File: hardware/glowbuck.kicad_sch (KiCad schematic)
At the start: 51 parts, among them J1 Conn_01x04_Socket, J101 Conn_01x01_Pin, J102 Conn_01x01_Pin, J105 Conn_01x01_Pin, J106 Conn_01x01_Pin, J107 Conn_01x01_Pin, J3 Conn_02x08_Counter_Clockwise, SW101 SW_Push, SW102 SW_Push, U101 ESP32-S3-WROOM-1

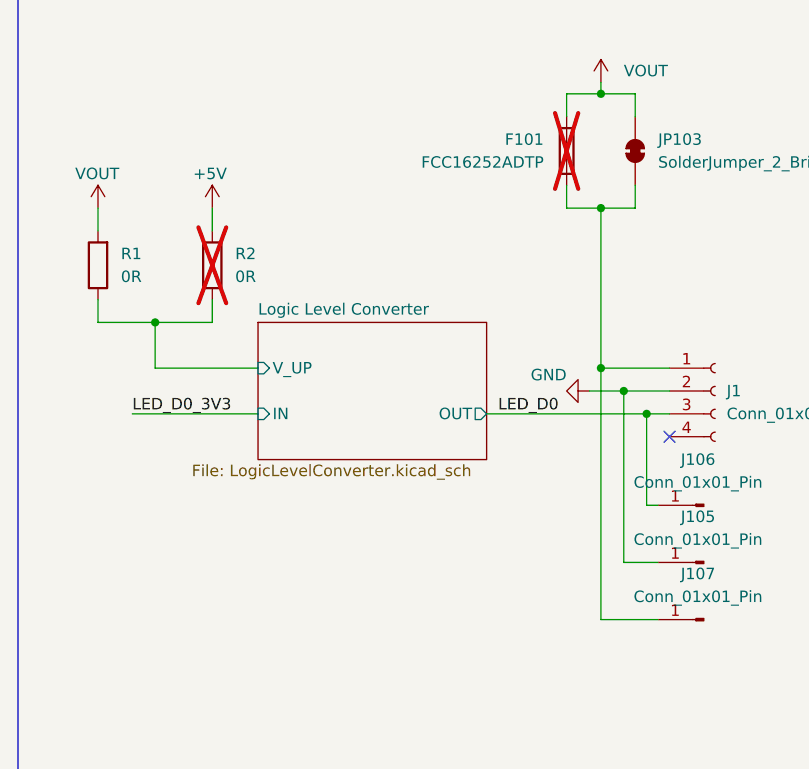
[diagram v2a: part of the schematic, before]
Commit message: Changed footprints to non hand solder option
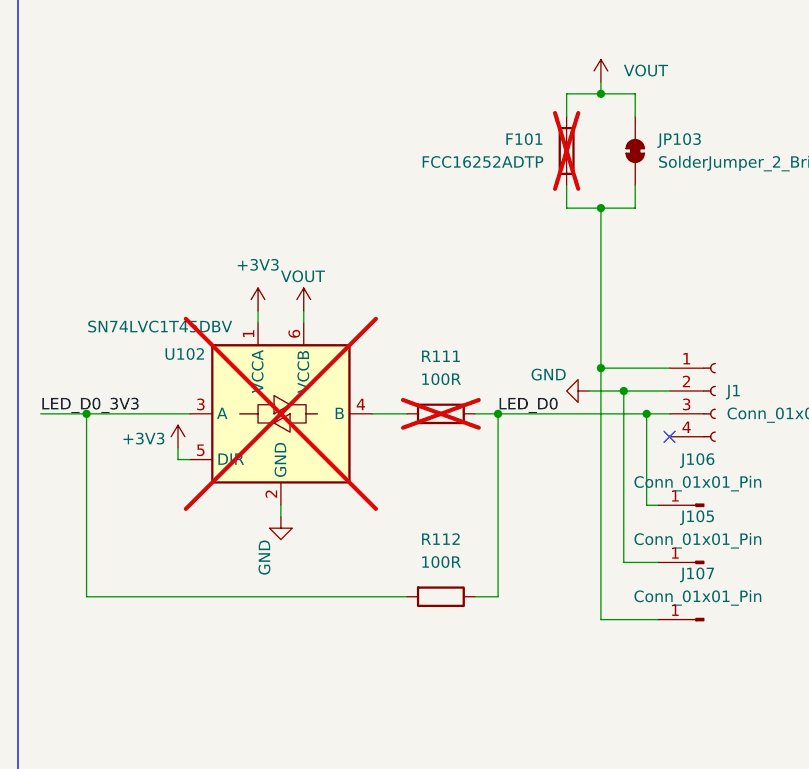
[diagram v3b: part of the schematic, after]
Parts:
- removed R1, R2: 0R, Resistor_SMD:R_0603_1608Metric_Pad0.98x0.95mm_HandSolder, symbol Device:R
- added R111, R112: 100R, Resistor_SMD:R_0603_1608Metric, symbol Device:R
- added U102: SN74LVC1T45DBV, Package_TO_SOT_SMD:SOT-23-6, symbol Logic_LevelTranslator:SN74LVC1T45DBV
- C101, C102, C103, C104, C105: footprint Capacitor_SMD:C_0603_1608Metric_Pad1.08x0.95mm_HandSolder -> Capacitor_SMD:C_0603_1608Metric
- D103: footprint LED_SMD:LED_0603_1608Metric_Pad1.05x0.95mm_HandSolder -> LED_SMD:LED_0603_1608Metric
- D104: footprint Diode_SMD:D_1206_3216Metric_Pad1.42x1.75mm_HandSolder -> Diode_SMD:D_1206_3216Metric
- R101, R102, R103, R104, R105, R106, R107, R108, R109, R110: footprint Resistor_SMD:R_0603_1608Metric_Pad0.98x0.95mm_HandSolder -> Resistor_SMD:R_0603_1608Metric
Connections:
- net +3V3: now also U102.1 (VCCA), U102.5 (DIR)
- net GND: now also U102.2 (GND)
- net LED_D0: now also R111.1, R112.1
- net LED_D0_3V3: now also R112.2, U102.3 (A)
- net VOUT: now also U102.6 (VCCB)
- new net: R111.2, U102.4 (B)
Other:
- removed sheet Logic Level Converter

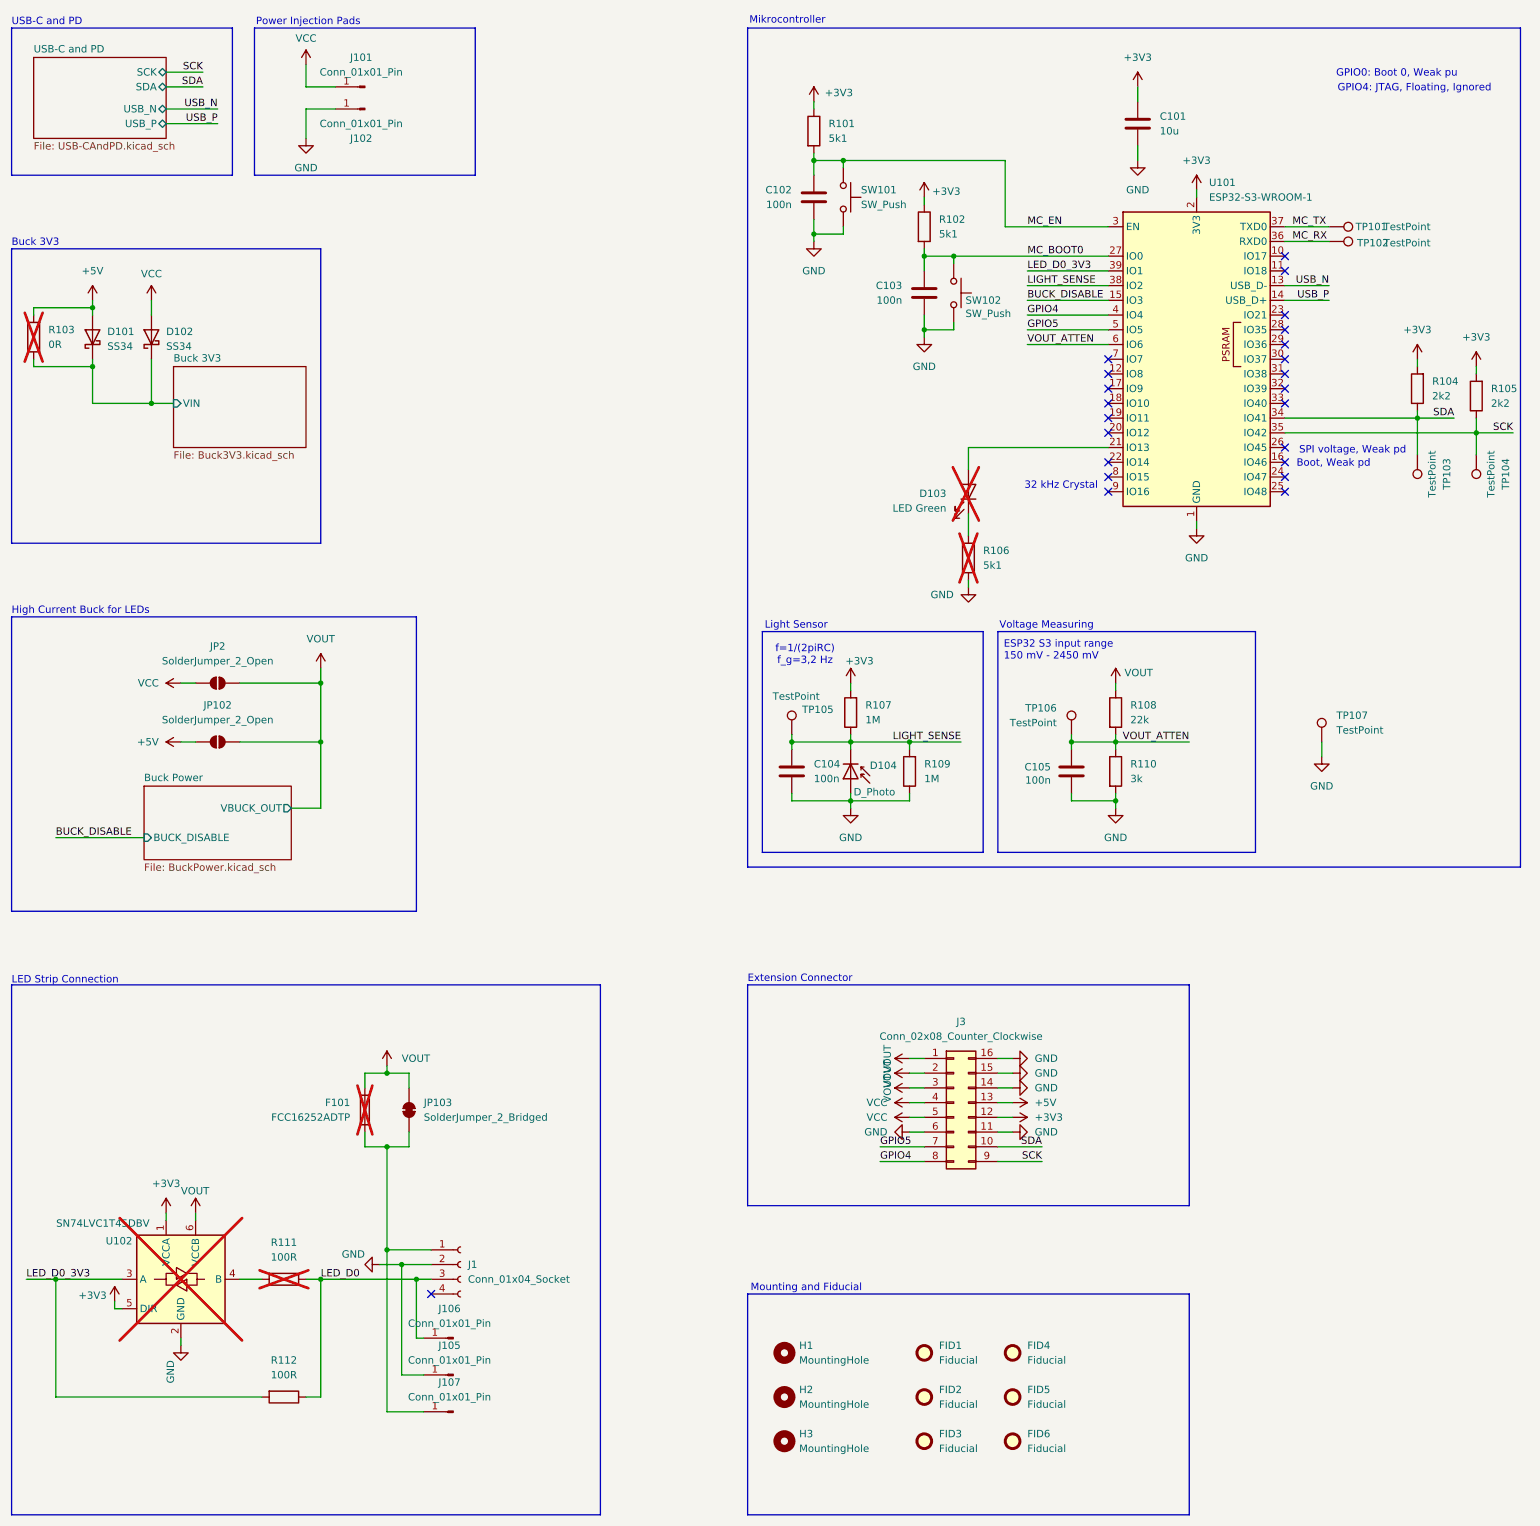
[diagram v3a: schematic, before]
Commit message: Colored nets and added optional current measurement
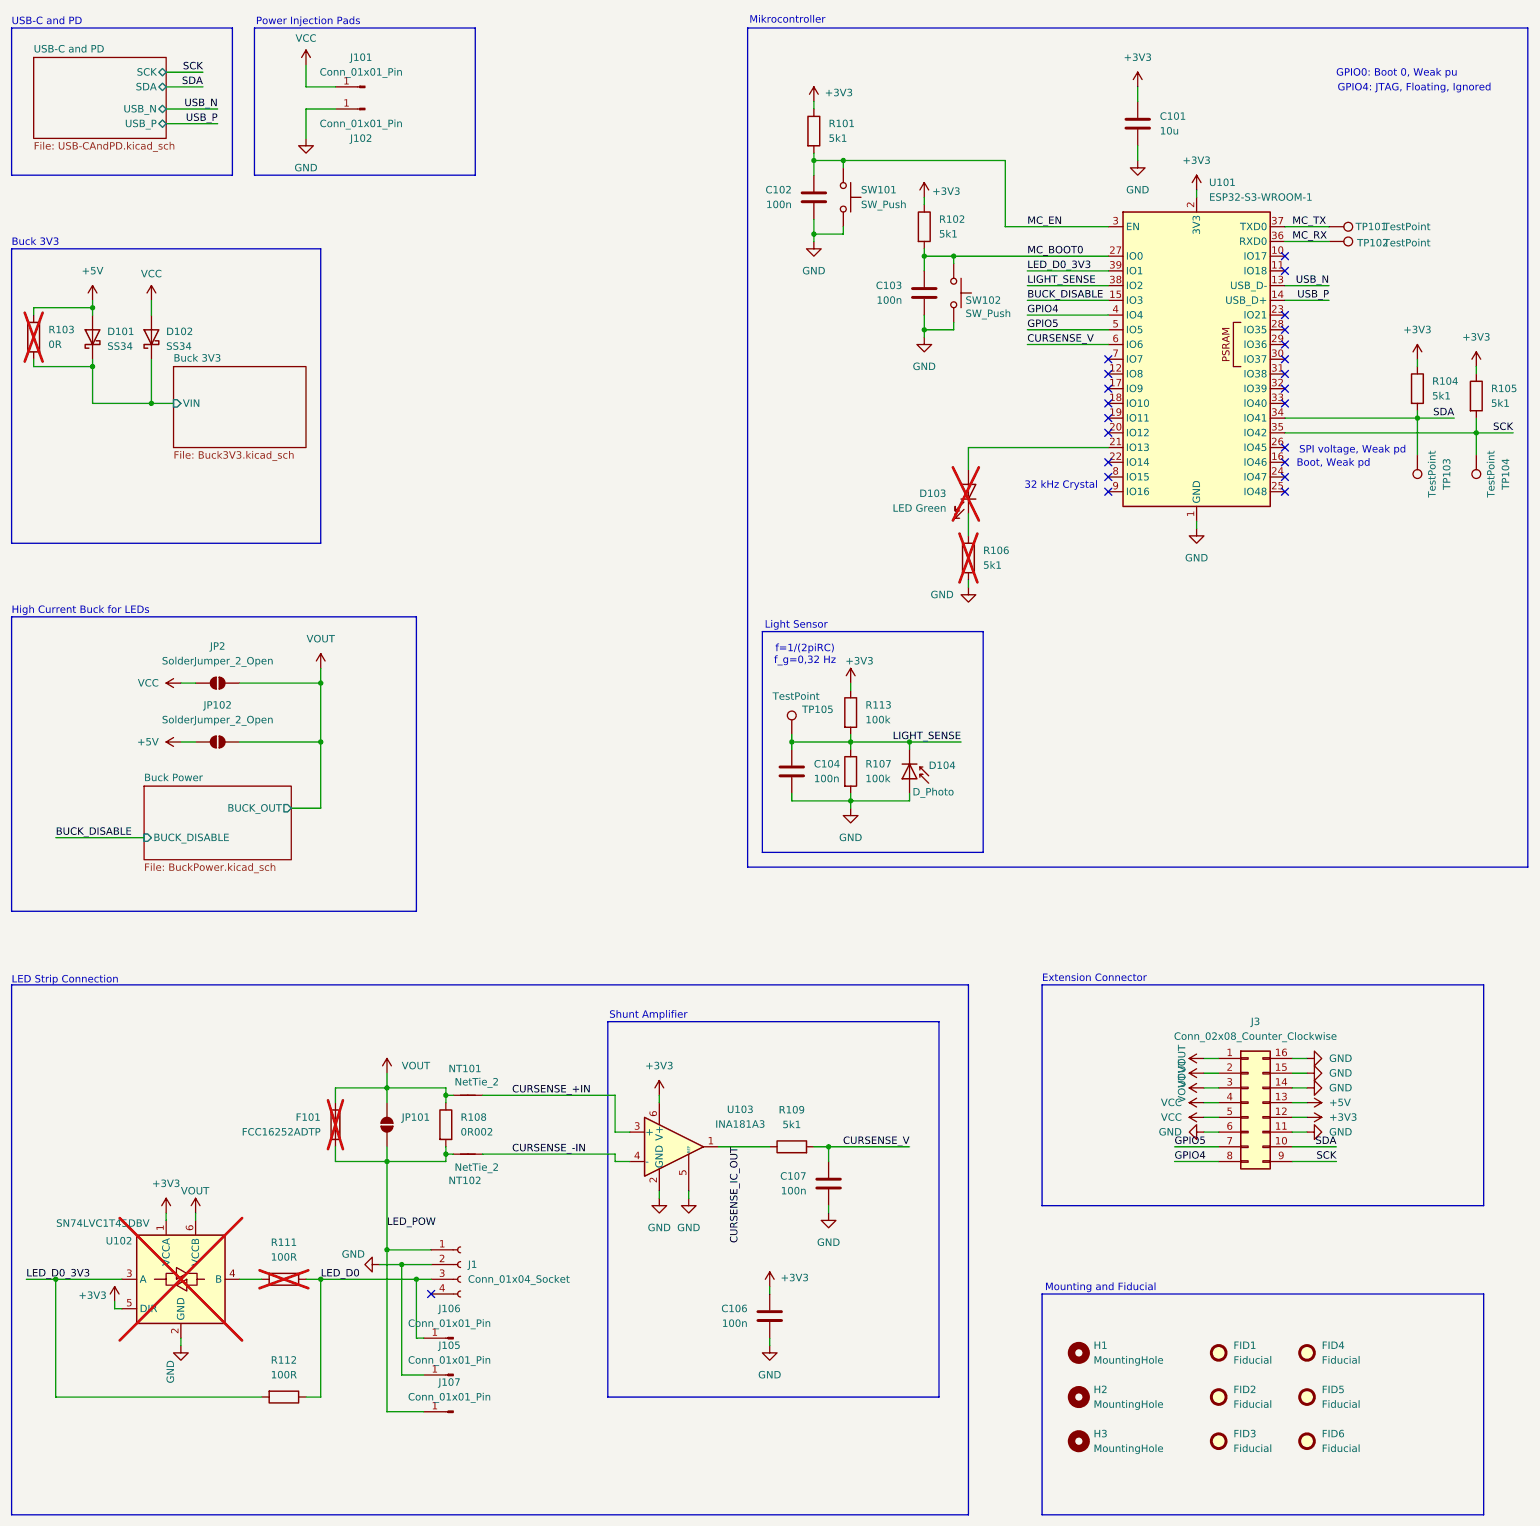
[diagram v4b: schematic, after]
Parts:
- removed C105: 100n, Capacitor_SMD:C_0603_1608Metric, symbol Device:C
- removed JP103: SolderJumper_2_Bridged, glowbuck:SolderJumper_Open_HighCurrent, symbol Jumper:SolderJumper_2_Bridged
- removed R110: 3k, Resistor_SMD:R_0603_1608Metric, symbol Device:R
- removed TP106, TP107: TestPoint, TestPoint:TestPoint_Pad_D1.0mm, symbol Connector:TestPoint
- added C106, C107: 100n, Capacitor_SMD:C_0603_1608Metric, symbol Device:C
- added JP101: SolderJumper_2_Open, glowbuck:SolderJumper_Open_HighCurrent, symbol Jumper:SolderJumper_2_Open
- added NT101, NT102: NetTie_2, glowbuck:NETTIE_0.3mm, symbol Device:NetTie_2
- added R113: 100k, Resistor_SMD:R_0603_1608Metric, symbol Device:R
- added U103: INA181A3, Package_TO_SOT_SMD:SOT-23-6, symbol Amplifier_Current:INA181
- R104, R105: value 2k2 -> 5k1; MouserNumber 603-RT0603DRE072K2L -> 652-CRT0603FZ1002ELF; now left out of the parts list
- R107: value 1M -> 100k; MouserNumber 603-RT0603FRD071ML -> 603-RT0603FRE07100KL
- R108: value 22k -> 0R002; ManufacturerNumber (none) -> WFC06032L000FE66; now left out of the parts list
- R109: value 1M -> 5k1; MouserNumber 603-RT0603FRD071ML -> 652-CRT0603FZ1002ELF; now left out of the parts list
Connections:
- net +3V3: now also R104.1, R105.1, C106.1, R113.1, U103.6 (V+); no longer R104.2, R105.2, R107.2
- net GND: now also R107.2, C106.2, C107.2, U103.2 (GND), U103.5 (REF); no longer R109.1
- net LIGHT_SENSE: now also R113.2; no longer R109.2
- net SCK: now also R105.2; no longer R105.1
- net SDA: now also R104.2; no longer R104.1
- net VOUT: now also JP101.2 (B), NT101.2
- net LED_POW: now reaches F101.1, J1.1 (Pin_1), J107.1 (Pin_1)
- net LED_POW: now also R108.2, JP101.1 (A), NT102.2
- net VOUT_ATTEN renamed CURSENSE_V
- net CURSENSE_V: now also R109.2, C107.1; no longer R108.2
- new net CURSENSE_+IN: NT101.1, U103.3 (+)
- new net CURSENSE_-IN: NT102.1, U103.4 (-)
- new net CURSENSE_IC_OUT: R109.1, U103.1
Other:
- sheet Buck Power ports: added BUCK_OUT; removed VBUCK_OUT
- note added: "Shunt Amplifier"
- note added: "f=1/(2piRC) f_g=0,32 Hz"
- note removed: "ESP32 S3 input range 150 mV - 2450 mV"
- note removed: "Voltage Measuring"
- note removed: "f=1/(2piRC) f_g=3,2 Hz"
- moved on the sheet: D104, F101, FID1, FID2, FID3, FID4, FID5, FID6, H1, H2, H3, J3

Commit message: Global labels, explanation texts, fix spring connector
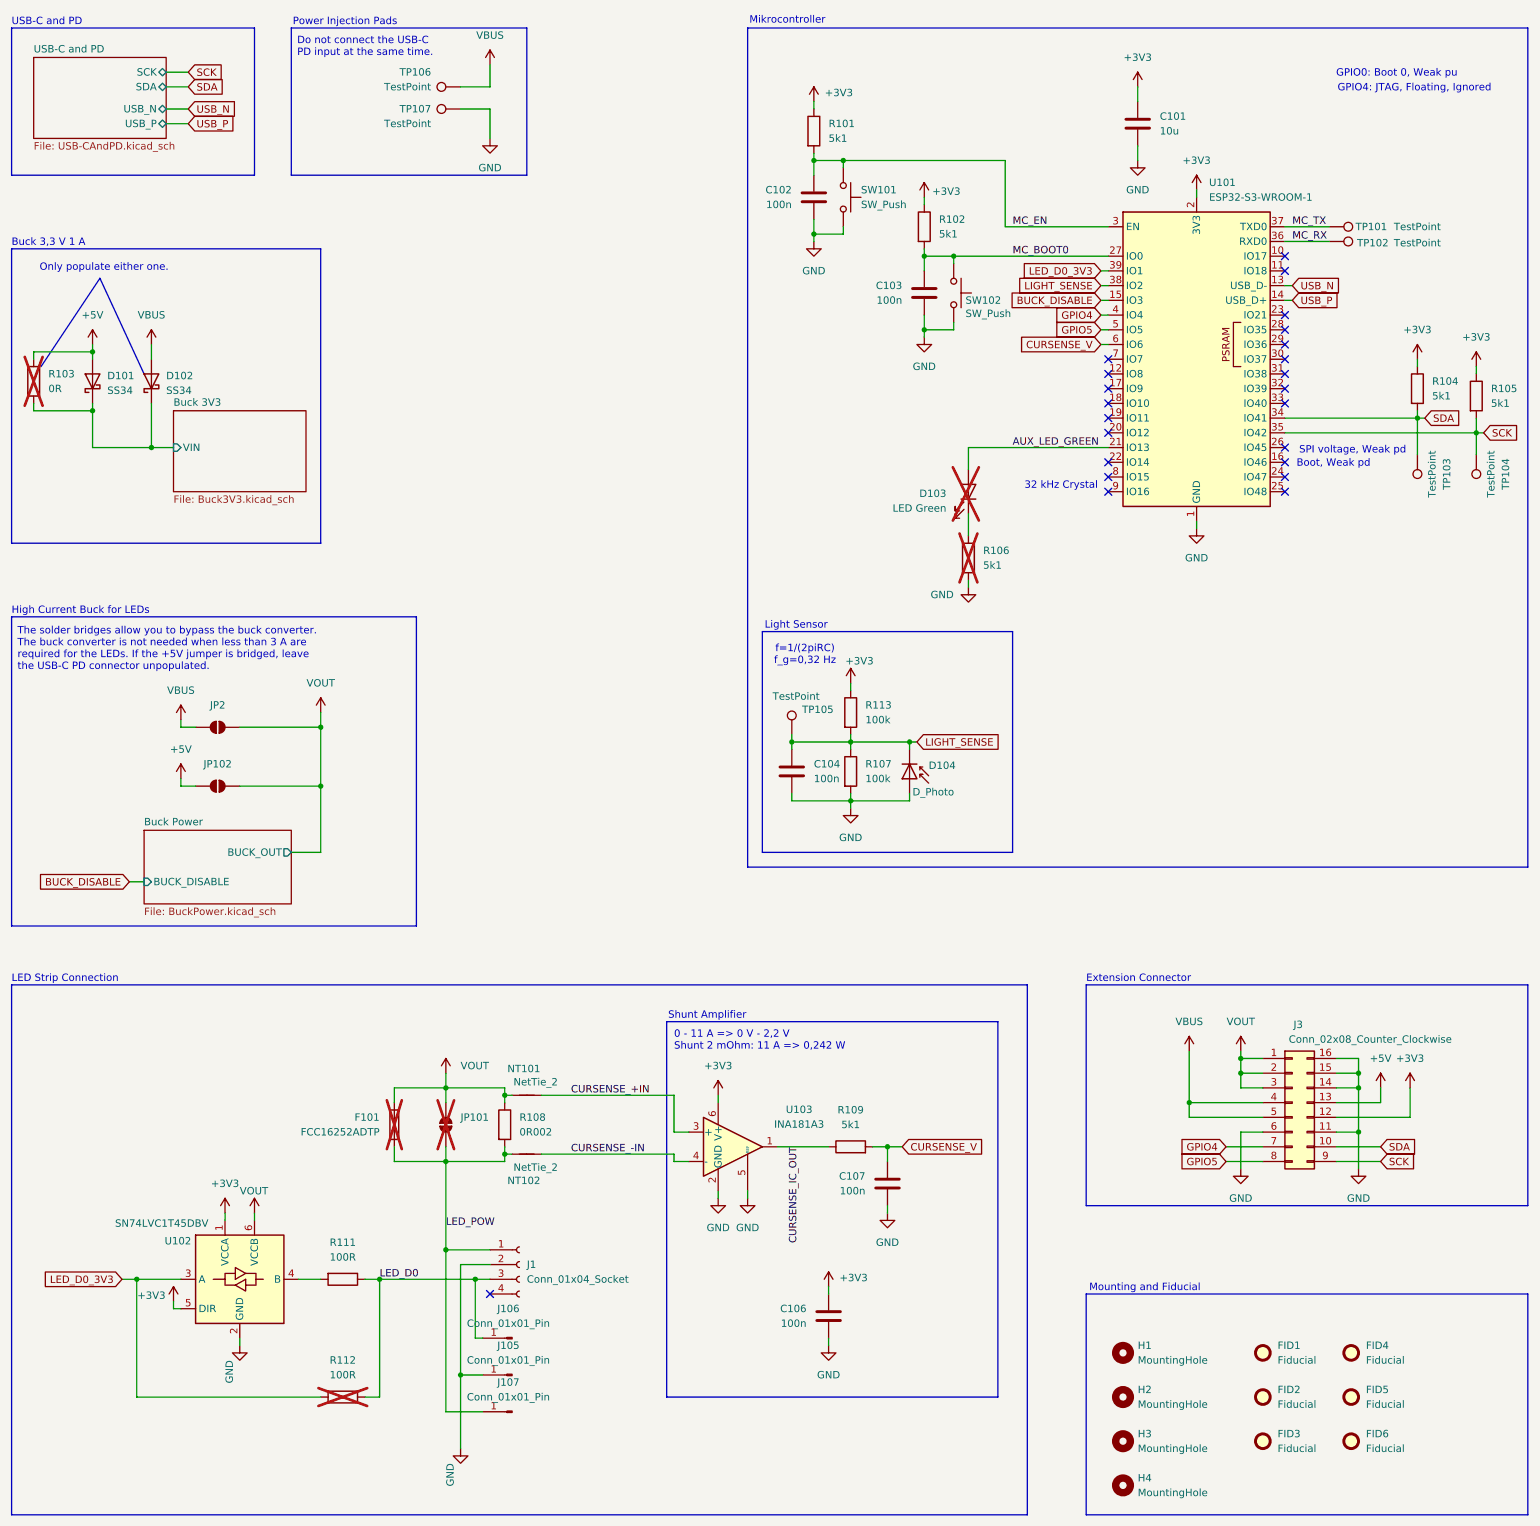
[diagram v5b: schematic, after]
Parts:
- removed J101, J102: Conn_01x01_Pin, TestPoint:TestPoint_Pad_3.0x3.0mm, symbol Connector:Conn_01x01_Pin
- added H4: MountingHole, MountingHole:MountingHole_2.2mm_M2_DIN965_Pad_TopBottom, symbol Mechanical:MountingHole
- added TP106, TP107: TestPoint, TestPoint:TestPoint_Pad_3.0x3.0mm, symbol Connector:TestPoint
- JP101, R112: now not fitted
- R111, U102: now fitted
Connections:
- net GND: now also TP107.1
- net GPIO4: now also J3.7 (Pin_7); no longer J3.8 (Pin_8)
- net GPIO5: now also J3.8 (Pin_8); no longer J3.7 (Pin_7)
- net AUX_LED_GREEN: now reaches D103.2 (A), U101.21 (IO13)
- net VCC renamed VBUS
- net VBUS: now also TP106.1
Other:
- note added: "0 - 11 A => 0 V - 2,2 V Shunt 2 mOhm: 11 A => 0,242 W"
- note added: "Buck 3,3 V 1 A"
- note added: "Do not connect the USB-C PD input at the same time."
- note added: "Only populate either one."
- note added: "The solder bridges allow you to bypass the buck converter. The buck converter is not needed when less than 3 A are required for the LEDs. If the +5V jumper is bridged, leave the USB-C PD connector unpopulated."
- note removed: "Buck 3V3"
- moved on the sheet: C106, C107, D101, D102, F101, FID1, FID2, FID3, FID4, FID5, FID6, H1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
